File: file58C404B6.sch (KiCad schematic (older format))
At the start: 53 parts

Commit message: Schematic complete
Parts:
- added D3, D4: TL4050B51, TO_SOT_Packages_SMD:SOT-23, symbol TL4050B51
- added R2: 333, Resistors_SMD:R_0603_HandSoldering, symbol R
- gave numbers to parts that had none: 47
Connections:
- net +15V: now also R2.1
- net 10V: now also D3.1 (K), R2.2
- net GND: now also P1.4, P2.4, U2.10 (+), U3.5 (+), D4.2 (A); no longer P1.2, P2.2, U2.3 (+), U3.3 (+)
- net at P1.1, R5.2: now also S1.1; no longer U2.3 (+)
- net at R19.2, S2.1: now also U2.8; no longer U2.1
- net at R17.2, R19.1: now also U2.9 (-); no longer U2.2 (-)
- net at R21.2, S3.1: now also U2.14; no longer U2.1
- net at R18.2, R21.1: now also U2.13 (-); no longer U2.2 (-)
- net at C12.1, C17.1, RV3.2: now also U2.12 (+); no longer U2.3 (+)
- net at R16.2, U5.1, U5.2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: now also U3.6 (-); no longer U3.2 (-)
- net at R3.1: now also P1.3; no longer P1.1
- net at S1.2: now also U2.5 (+); no longer P2.1
- net at R17.1, R20.1, S2.3: now also U3.7; no longer U3.1
- new net: P2.3, U2.6 (-), U2.7
- new net: D3.2 (A), D4.1 (K)
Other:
- moved on the sheet: C10, C8, S1

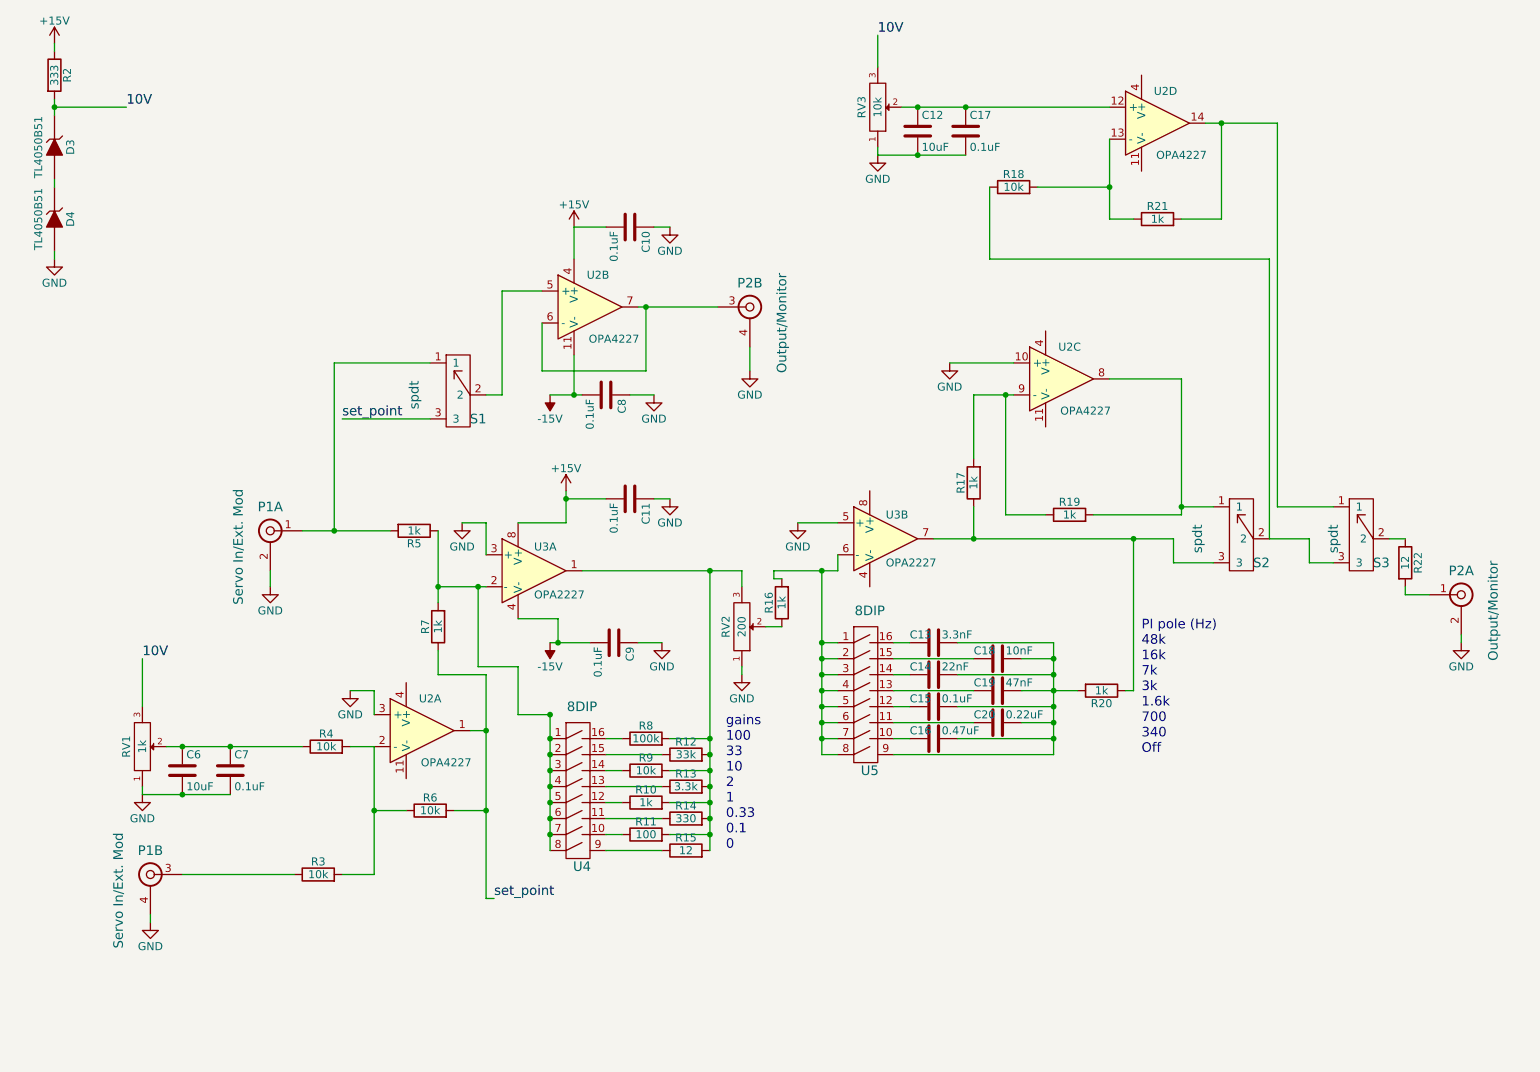
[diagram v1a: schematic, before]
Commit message: Made both circiuts identical
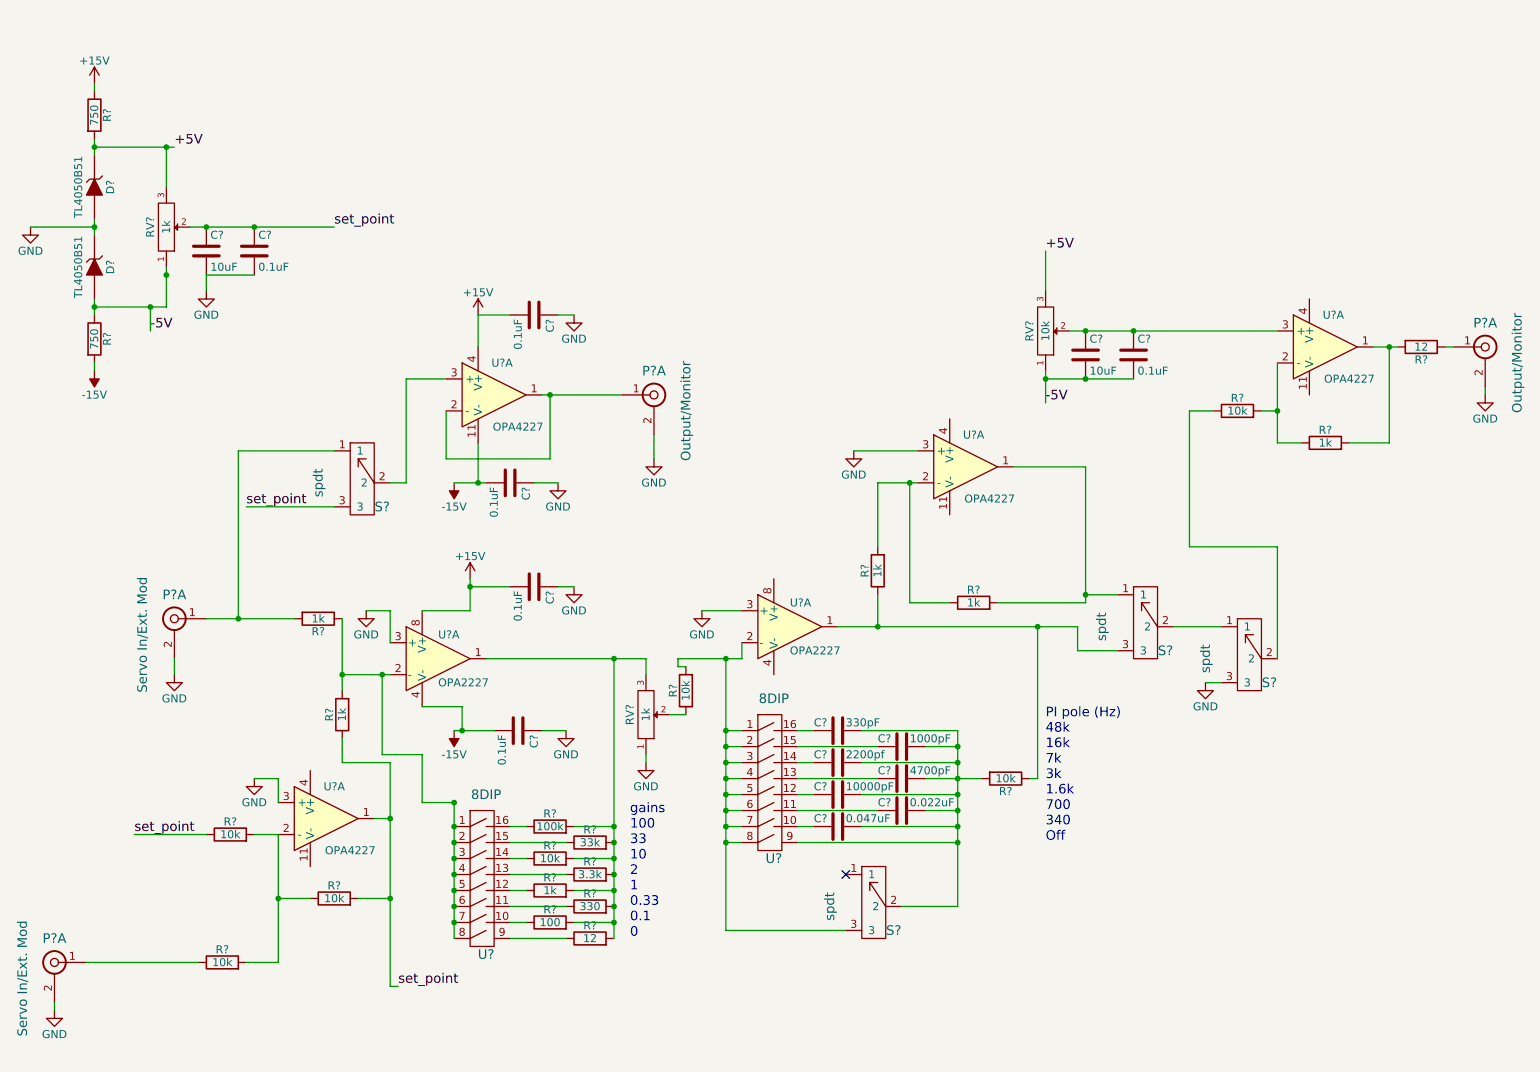
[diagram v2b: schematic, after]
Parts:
- removed C10, C11, C15, C17, C7, C8, C9: 0.1uF, Capacitors_SMD:C_0603_HandSoldering, symbol C
- removed C12, C6: 10uF, Capacitors_SMD:C_0603_HandSoldering, symbol C
- removed C13: 3.3nF, Capacitors_SMD:C_0603_HandSoldering, symbol C
- removed C14: 22nF, Capacitors_SMD:C_0603_HandSoldering, symbol C
- removed C16: 0.47uF, Capacitors_SMD:C_0603_HandSoldering, symbol C
- removed C18: 10nF, Capacitors_SMD:C_0603_HandSoldering, symbol C
- removed C19: 47nF, Capacitors_SMD:C_0603_HandSoldering, symbol C
- removed C20: 0.22uF, Capacitors_SMD:C_0603_HandSoldering, symbol C
- removed D3, D4: TL4050B51, TO_SOT_Packages_SMD:SOT-23, symbol TL4050B51
- removed P1: Servo In/Ext. Mod, symbol Dual-BNC
- removed P2: Output/Monitor, footprints:Dual-BNC-ARF2136, symbol Dual-BNC
- removed R10, R16, R17, R19, R20, R21, R5, R7: 1k, Resistors_SMD:R_0603_HandSoldering, symbol R
- removed R11: 100, Resistors_SMD:R_0603_HandSoldering, symbol R
- removed R12: 33k, Resistors_SMD:R_0603_HandSoldering, symbol R
- removed R13: 3.3k, Resistors_SMD:R_0603_HandSoldering, symbol R
- removed R14: 330, Resistors_SMD:R_0603_HandSoldering, symbol R
- removed R15, R22: 12, Resistors_SMD:R_0603_HandSoldering, symbol R
- removed R18, R3, R4, R6, R9: 10k, Resistors_SMD:R_0603_HandSoldering, symbol R
- removed R2: 333, Resistors_SMD:R_0603_HandSoldering, symbol R
- removed R8: 100k, Resistors_SMD:R_0603_HandSoldering, symbol R
- removed RV1: 1k, footprints:VishaySpectrol536, symbol POT
- removed RV2: 200, symbol POT
- removed RV3: 10k, footprints:Bourns-PV36W104C01B00-trimmer, symbol POT
- removed S1, S2, S3: spdt, footprints:CJS-1200TB-SPDT, symbol spdt
- removed U2: OPA4227, Housings_SOIC:SOIC-14_3.9x8.7mm_Pitch1.27mm, symbol OPA4227
- removed U3: OPA2227, Housings_SOIC:SOIC-8_3.9x4.9mm_Pitch1.27mm, symbol OPA2227
- removed U4, U5: 8DIP, footprints:8_POS_DIP_Switch, symbol 8DIP
- added C? (x6): 0.1uF, symbol C
- added C?: 330pF, symbol C
- added C?: 1000pF, symbol C
- added C?: 2200pf, symbol C
- added C?: 4700pF, symbol C
- added C?: 10000pF, symbol C
- added C?: 0.022uF, symbol C
- added C?: 0.047uF, symbol C
- added C? (x2): 10uF, symbol C
- added D? (x2): TL4050B51, symbol TL4050B51
- added P? (x2): Output/Monitor, symbol Dual-BNC
- added P? (x2): Servo In/Ext. Mod, symbol Dual-BNC
- added R? (x6): 1k, symbol R
- added R?: 100k, symbol R
- added R?: 33k, symbol R
- added R? (x7): 10k, symbol R
- added R?: 3.3k, symbol R
- added R?: 330, symbol R
- added R?: 100, symbol R
- added R? (x2): 12, symbol R
- added R? (x2): 750, symbol R
- added RV?: 10k, symbol POT
- added RV? (x2): 1k, symbol POT
- added S? (x4): spdt, symbol spdt
- added U? (x4): OPA4227, symbol OPA4227
- added U? (x2): 8DIP, symbol 8DIP
- added U? (x2): OPA2227, symbol OPA2227
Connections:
- net +15V: now also C?.2, C?.2, R?.1, U?.4 (V+), U?.8 (V+)
- net -15V: now also C?.2, C?.2, R?.2, U?.11 (V-), U?.4 (V-)
- net GND: now also C?.1, C?.1, C?.1, C?.1, C?.2, C?.2, D?.1 (K), D?.2 (A), P?.2, P?.2, P?.2, P?.2, RV?.1, S?.3, U?.3 (+), U?.3 (+), U?.3 (+), U?.3 (+)
- net set_point: now also C?.1, C?.1, R?.1, R?.1, R?.2, RV?.2, S?.3, U?.1
- new net: P?.1, U?.1, U?.2 (-)
- new net: S?.2, U?.3 (+)
- new net: R?.2, S?.1, U?.1
- new net: R?.1, R?.2, U?.2 (-) (x2)
- new net: R?.1, R?.2, R?.2, U?.2 (-)
- new net: R?.2, R?.2, U?.1
- new net: C?.1, C?.1, RV?.2, U?.3 (+)
- new net: R?.1, R?.2, U?.1, U?.2, U?.2 (-), U?.3, U?.4, U?.5, U?.6, U?.7, U?.8
- new net: P?.1, R?.2, S?.1
- new net: R?.1, U?.10
- new net: R?.1, U?.11
- new net: R?.1, U?.12
- new net: R?.1, U?.13
- new net: R?.1, U?.14
- new net: R?.1, U?.15
- new net: R?.1, U?.16
- new net: R?.1, U?.9
- new net: R?.2, R?.2, R?.2, R?.2, R?.2, R?.2, R?.2, R?.2, RV?.3, U?.1
- new net: R?.2, S?.3, U?.1, U?.2, U?.2 (-), U?.3, U?.4, U?.5, U?.6, U?.7, U?.8
- new net: C?.2, U?.10
- new net: C?.2, U?.11
- new net: C?.2, U?.12
- new net: C?.2, U?.13
- new net: C?.2, U?.14
- new net: C?.2, U?.15
- new net: C?.2, U?.16
- new net: C?.1, C?.1, C?.1, C?.1, C?.1, C?.1, C?.1, R?.2, S?.2, U?.9
- new net: R?.1, RV?.2
- new net: P?.1, R?.1 (x2)
- new net: R?.1, R?.1, S?.3, U?.1
- new net: S?.1, S?.2
- new net: R?.1, S?.2
- new net +5V: D?.1 (K), R?.2, RV?.3, RV?.3
- new net -5V: C?.2, C?.2, D?.2 (A), R?.1, RV?.1, RV?.1
- no-connect marks 0 -> 1

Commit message: Footprints assigned
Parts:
- gave numbers to parts that had none: 52
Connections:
- net GND: now also P1.4, P2.4, U2.10 (+), U3.5 (+); no longer P1.2, P2.2, U2.3 (+), U3.3 (+)
- net at S1.2: now also U2.5 (+); no longer U2.3 (+)
- net at R18.2, S3.1: now also U2.8; no longer U2.1
- net at R17.2, R18.1: now also U2.9 (-); no longer U2.2 (-)
- net at R21.2, R22.2: now also U2.14; no longer U2.1
- net at R20.2, R21.1: now also U2.13 (-); no longer U2.2 (-)
- net at C19.1, C20.1, RV3.2: now also U2.12 (+); no longer U2.3 (+)
- net at R5.2, S1.1: now also P1.1; no longer P1.1
- net at R16.2, S2.3, U5.1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: now also U3.6 (-); no longer U3.2 (-)
- net at R22.1: now also P2.1; no longer P2.1
- net at R3.1: now also P1.3; no longer P1.1
- net at R17.1, R19.1, S3.3: now also U3.7; no longer U3.1
- new net: P2.3, U2.6 (-), U2.7
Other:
- moved on the sheet: P1A, P2A

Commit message: Board connectors placed
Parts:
- C10, C11, C12, C13, C14, C15, C16, C17, C18, C19, C20, C6, C7, C8, C9: footprint (none) -> Capacitors_SMD:C_0805_HandSoldering
- D1, D2: footprint (none) -> TO_SOT_Packages_SMD:SOT-23
- P1, P2: footprint (none) -> footprints:Dual-BNC-ARF2136
- R1, R10, R11, R12, R13, R14, R15, R16, R17, R18, R19, R2, R20, R21, R22, R3, R4, R5, R6, R7, R8, R9: footprint (none) -> Resistors_SMD:R_0805_HandSoldering
- RV1, RV2, RV3: footprint (none) -> footprints:VishaySpectrol536
- S1, S2, S3, S4: footprint (none) -> footprints:SPDT-Horizontal
- U2: footprint (none) -> Housings_SOIC:SOIC-14_3.9x8.7mm_Pitch1.27mm
- U3: footprint (none) -> Housings_SOIC:SOIC-8_3.9x4.9mm_Pitch1.27mm
- U4, U5: footprint (none) -> footprints:8_POS_DIP_Switch

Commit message: PI circuit 1 done
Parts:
- S3: footprint footprints:SPDT-Horizontal -> footprints:CJS-1200TB-SPDT
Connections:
- net -5V: no longer C19.2, C20.2
- net GND: now also C19.2, C20.2
- net set_point: no longer R6.2, R7.1, S1.3, U2.1
- new net set_point_mon: R6.2, R7.1, S1.3, U2.1
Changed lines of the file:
@@
 F 0 "S3" V 8200 4400 60  0000 C CNN
 F 1 "spdt" H 8050 4800 60  0000 C CNN
-F 2 "footprints:SPDT-Horizontal" H 8050 4550 60  0001 C CNN
+F 2 "footprints:CJS-1200TB-SPDT" H 8050 4550 60  0001 C CNN
 F 3 "" H 8050 4550 60  0000 C CNN
 	1    8050 4550
@@
 Connection ~ 7700 2700
 Connection ~ 8000 2700
-Wire Wire Line
-	7450 3000 8000 3000
 Connection ~ 7700 3000
 Wire Wire Line
@@
 Wire Wire Line
 	1450 6650 2150 6650
-Text Label 3400 6800 0    60   ~ 0
-set_point
-Wire Wire Line
-	3350 6800 3400 6800
-Text Label 2450 3800 0    60   ~ 0
-set_point
-Wire Wire Line
-	2450 3800 3000 3800
+Text Label 1700 3800 0    60   ~ 0
+set_point_mon
+Wire Wire Line
+	3350 6800 3450 6800
+Wire Wire Line
+	1700 3800 3000 3800
 $Comp
 L POT RV2
@@
 Wire Wire Line
 	8350 4050 8350 3200
+Text Label 3450 6800 0    60   ~ 0
+set_point_mon
+$Comp
+L GND #PWR?
+U 1 1 58C7F4CC
+P 7750 3100
+F 0 "#PWR?" H 7750 2850 50  0001 C CNN
+F 1 "GND" H 7750 2950 50  0000 C CNN
+F 2 "" H 7750 3100 50  0000 C CNN
+F 3 "" H 7750 3100 50  0000 C CNN
+	1    7750 3100
+	1    0    0    -1
+$EndComp
+Wire Wire Line
+	7750 3000 7750 3100
+Connection ~ 7750 3000
+Wire Wire Line
+	7700 3000 8000 3000
 $EndSCHEMATC

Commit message: Track routing done.
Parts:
- RV1, RV2, RV3: symbol POT -> POT-RESCUE-mini_pid
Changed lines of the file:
@@
 EESchema Schematic File Version 2
+LIBS:mini_pid-rescue
 LIBS:power
 LIBS:device
@@
 $EndComp
 $Comp
-L POT RV3
+L POT-RESCUE-mini_pid RV3
 U 1 1 58CABA7A
 P 7450 2700
+AR Path="/58CABA7A" Ref="RV3"  Part="1"
+AR Path="/58C404B7/58CABA7A" Ref="RV3"  Part="1"
 F 0 "RV3" H 7450 2600 50  0000 C CNN
 F 1 "10k" H 7450 2700 50  0000 C CNN
@@
 	1700 3800 3000 3800
 $Comp
-L POT RV2
+L POT-RESCUE-mini_pid RV2
 U 1 1 58CABB75
 P 4950 5100
+AR Path="/58CABB75" Ref="RV2"  Part="1"
+AR Path="/58C404B7/58CABB75" Ref="RV2"  Part="1"
 F 0 "RV2" H 4950 5000 50  0000 C CNN
 F 1 "1k" H 4950 5100 50  0000 C CNN
@@
 	3450 3650 3450 3000
 $Comp
-L POT RV1
+L POT-RESCUE-mini_pid RV1
 U 1 1 58CABB8B
 P 1950 2050
+AR Path="/58CABB8B" Ref="RV1"  Part="1"
+AR Path="/58C404B7/58CABB8B" Ref="RV1"  Part="1"
 F 0 "RV1" H 1950 1950 50  0000 C CNN
 F 1 "1k" H 1950 2050 50  0000 C CNN
